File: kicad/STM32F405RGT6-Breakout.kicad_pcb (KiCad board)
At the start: 4 copper layers, 60 parts, among them J1 USB_C_Receptacle_USB2.0, J2 PWR OUT, J3 SWD/JTAG, J4 USART6, J5 SPI1, J6 I2C1, J7 I2C2, Q1 Si2301CDS, SW1 TS-1187A-B-A-B, SW2 TS-1187A-B-A-B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

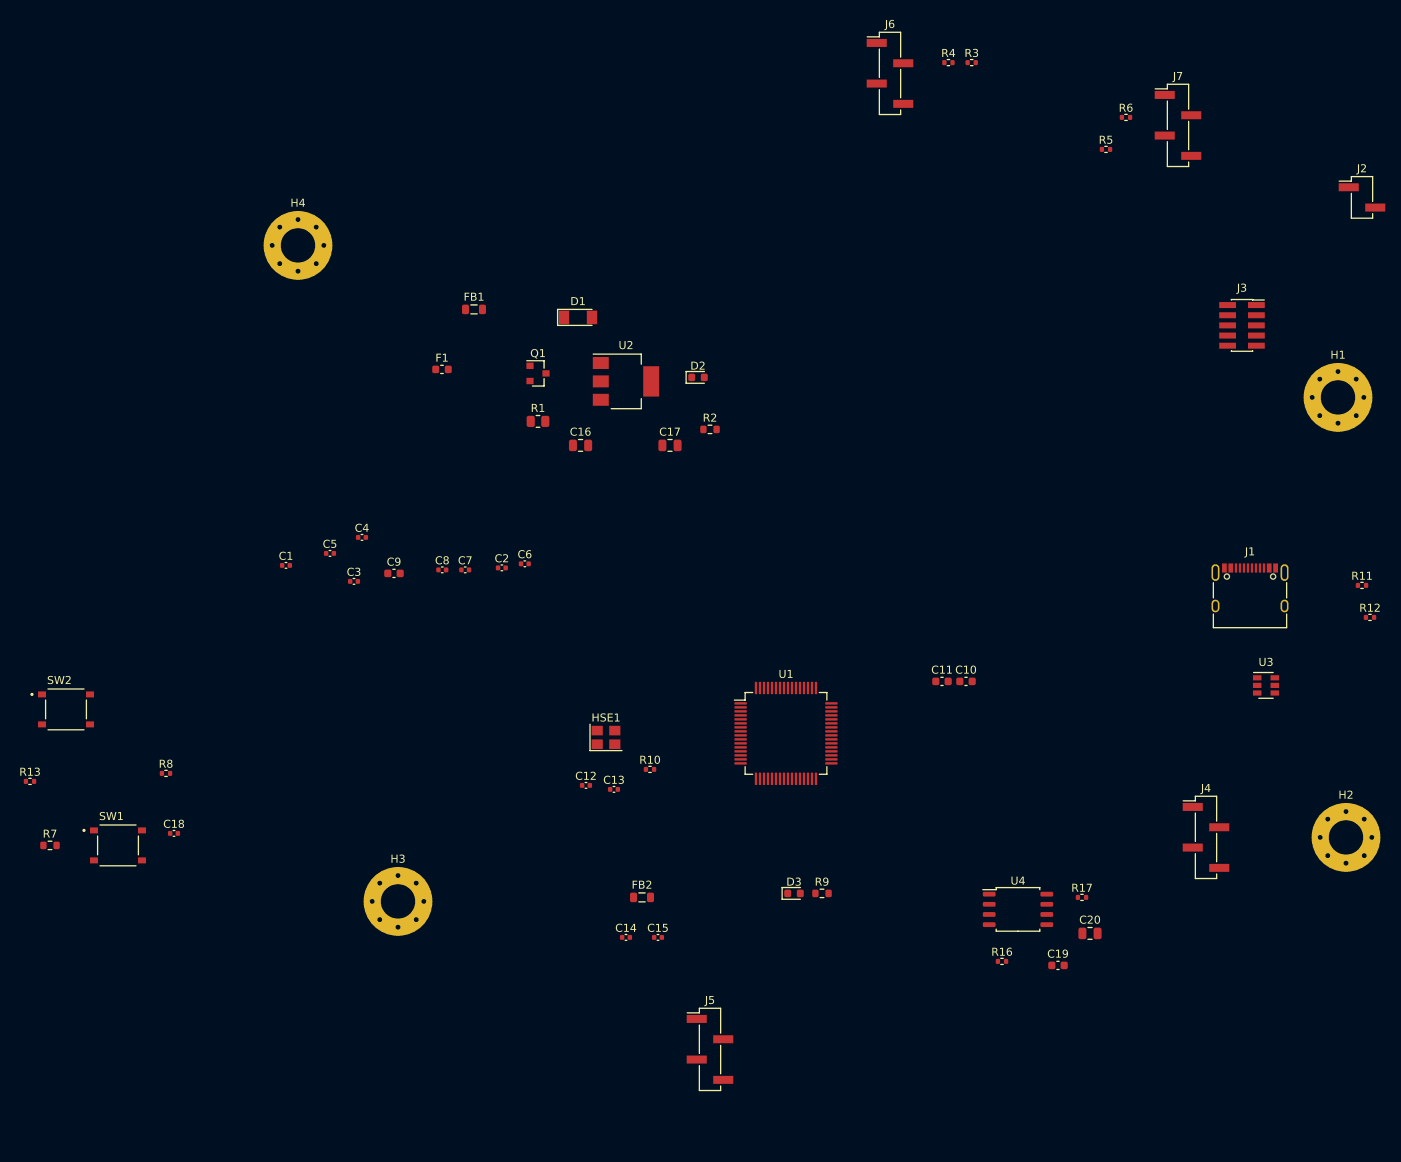
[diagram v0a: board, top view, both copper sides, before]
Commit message: - Laid out & routed crystal - Laid out & started routing MCU decoupling
--> Checkpoint before trying new flash orientation
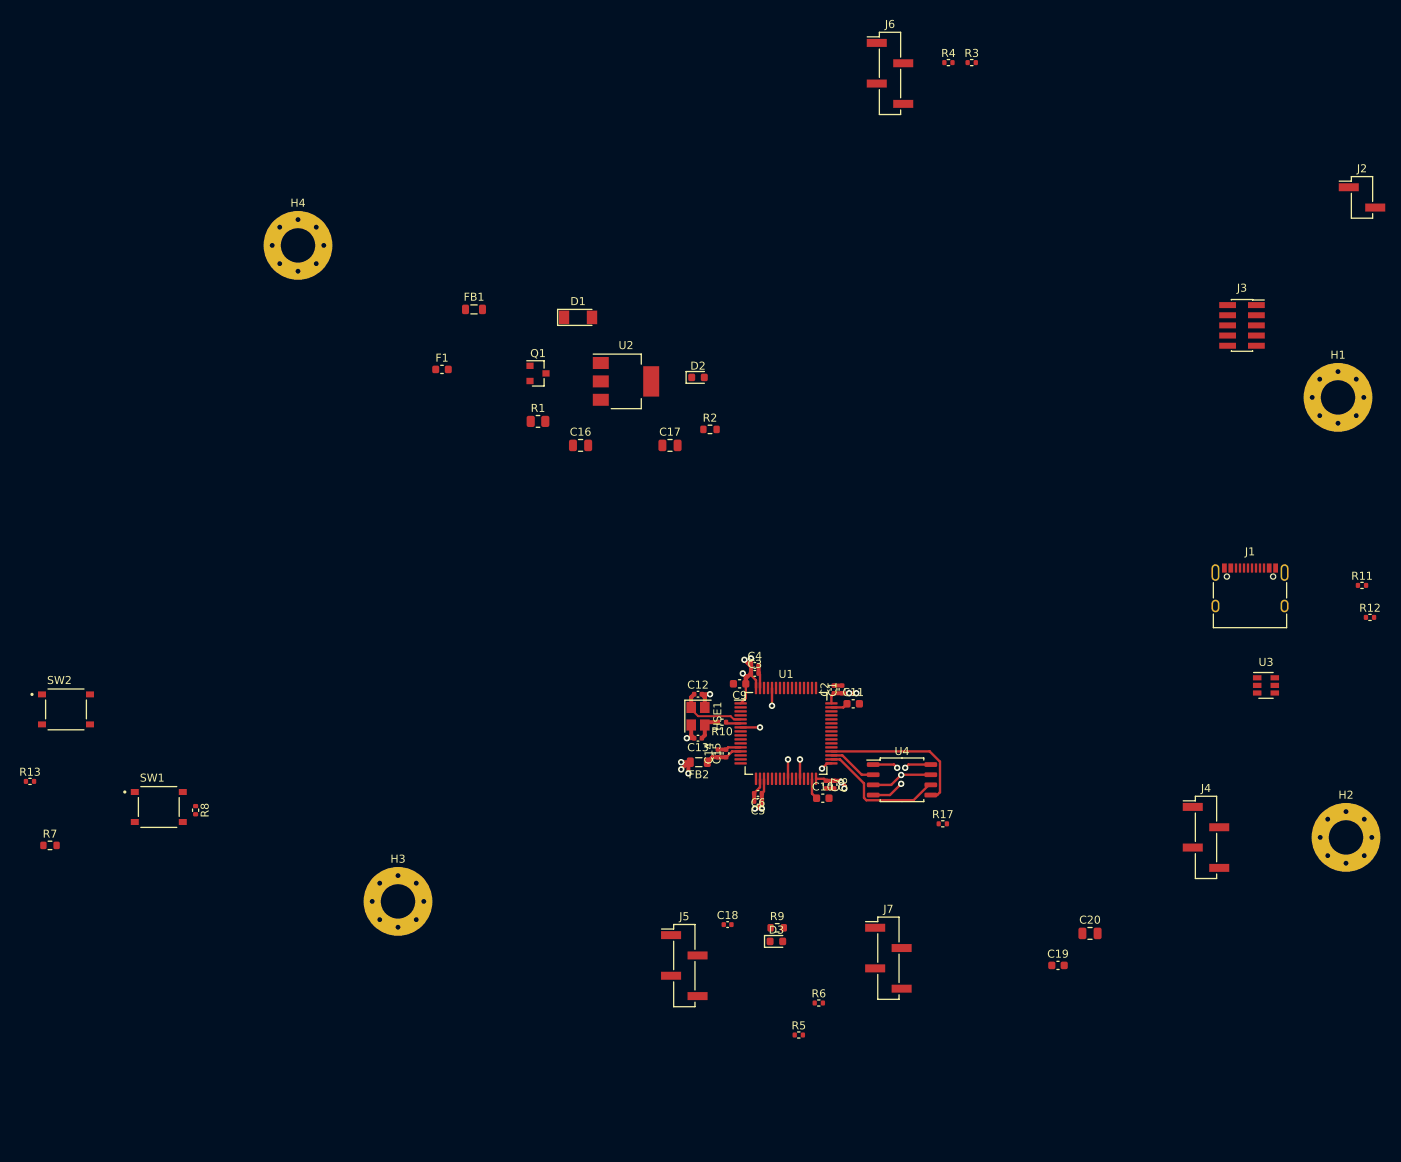
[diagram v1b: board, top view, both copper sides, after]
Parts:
- removed R16: 10k, Resistor_SMD:R_0402_1005Metric
- moved R5 117.2 mm to (123.6, 122.7)
- moved R6 117.2 mm to (126.1, 118.7)
- moved J7 110.2 mm to (134.8, 113.1)
- moved C1 71.2 mm to (129.0, 79.5), turned to 90 degrees
- moved C18 70.1 mm to (114.7, 108.9)
- moved C5 61.8 mm to (118.5, 93.5), turned to 180 degrees
- moved C8 55.8 mm to (128.0, 91.4), turned to 270 degrees
- moved C7 52.5 mm to (127.0, 91.4), turned to 270 degrees
- moved C4 51.6 mm to (118.1, 76.5)
- moved C3 51.4 mm to (118.1, 77.5)
- moved C9 45.4 mm to (116.2, 78.8), turned to 180 degrees
- moved C2 44.2 mm to (128.0, 79.5), turned to 90 degrees
- moved C6 40.9 mm to (118.5, 92.5), turned to 180 degrees
- moved C14 25.7 mm to (113.5, 87.5), turned to 90 degrees
- moved C15 24.5 mm to (114.5, 87.5), turned to 90 degrees
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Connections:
- R17 pad 1: Net-(R17-Pad1) -> GND
- R17 pad 2: GND -> Net-(R17-Pad2)
- U4 pad 3: Net-(R16-Pad2) -> Net-(R17-Pad2)
- U4 pad 7: Net-(R17-Pad1) -> Net-(R17-Pad2)
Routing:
- net +3V3: track 0.00 -> 32.1 mm, vias 0 -> 13
- net GND: track 0.00 -> 20.7 mm, vias 0 -> 3
- net FLASH_MOSI: track 0.00 -> 19.2 mm
- net FLASH_SCK: track 0.00 -> 16.4 mm
- net HSE_IN: track 0.00 -> 8.73 mm
- net Net-(R17-Pad2): track 0.00 -> 7.73 mm, vias 0 -> 1
- net FLASH_MISO: track 0.00 -> 6.23 mm
- net +3.3VA: track 0.00 -> 4.72 mm
- net FLASH_CS: track 0.00 -> 4.61 mm, vias 0 -> 2
- net Net-(C13-Pad1): track 0.00 -> 3.59 mm
- net Net-(C10-Pad1): track 0.00 -> 2.66 mm
- net Net-(D3-Pad2): track 0.00 -> 2.42 mm, vias 0 -> 1
- net NRST: track 0.00 -> 2.42 mm, vias 0 -> 1
- net BOOT1: track 0.00 -> 2.42 mm, vias 0 -> 1
- net BOOT0: track 0.00 -> 2.22 mm, vias 0 -> 1
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- added copper zone on In1.Cu, net GND
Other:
- net class 3V3 added: clearance 0.2, trace_width 0.5, via_dia 0.8, via_drill 0.4
- net class 5V added: clearance 0.2, trace_width 1, via_dia 0.8, via_drill 0.4

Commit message: This flash SPI routing is definitely better
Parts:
- moved R17 7.83 mm to (142.3, 88.5), turned to 180 degrees
- moved U4 1.70 mm to (136.5, 89.1), turned to 180 degrees
- moved C10 0.10 mm to (126.5, 93.1)
- moved C7 0.10 mm to (126.9, 91.4)
- moved C8 0.10 mm to (127.9, 91.4)
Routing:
- net FLASH_MOSI: track 19.2 -> 5.25 mm
- net FLASH_MISO: track 6.23 -> 17.7 mm
- net FLASH_SCK: track 16.4 -> 5.31 mm
- net GND: track 20.7 -> 16.6 mm, vias 3 -> 2
- net Net-(R17-Pad2): track 7.73 -> 9.67 mm, vias 1 -> 0
- net +3V3: track 32.1 -> 30.2 mm
- net FLASH_CS: track 4.61 -> 6.40 mm

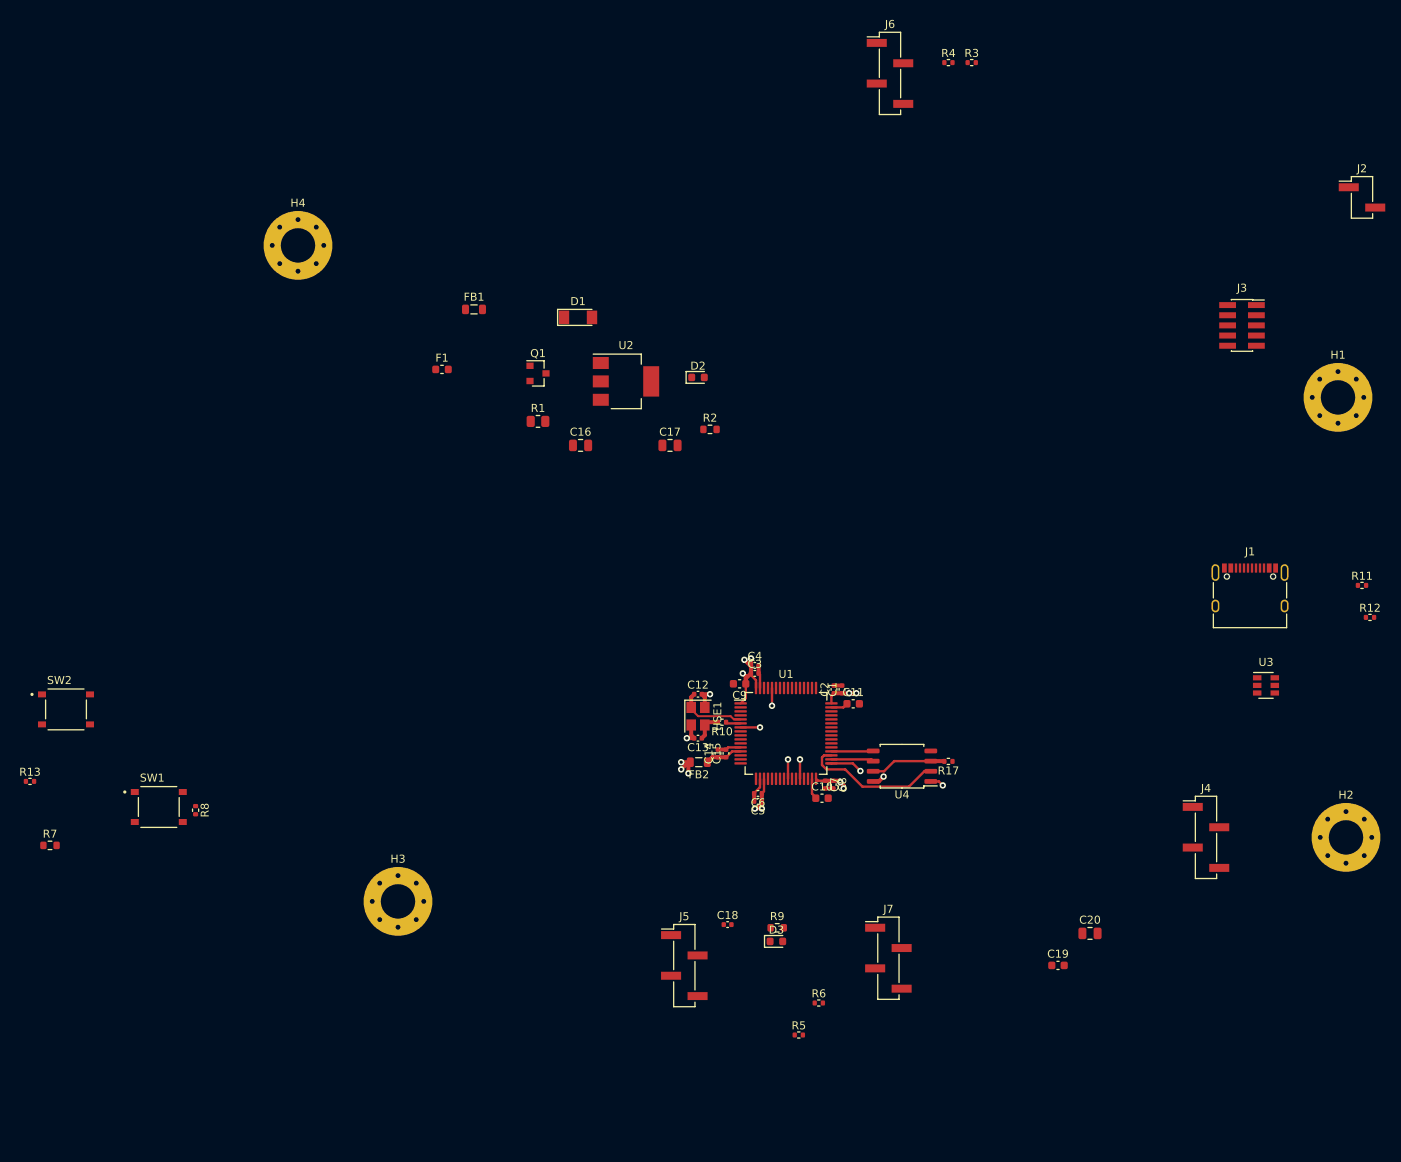
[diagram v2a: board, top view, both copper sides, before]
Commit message: - USB connector & ESD protection laid out - Crystal moved to make room for fanning out GPIO pins
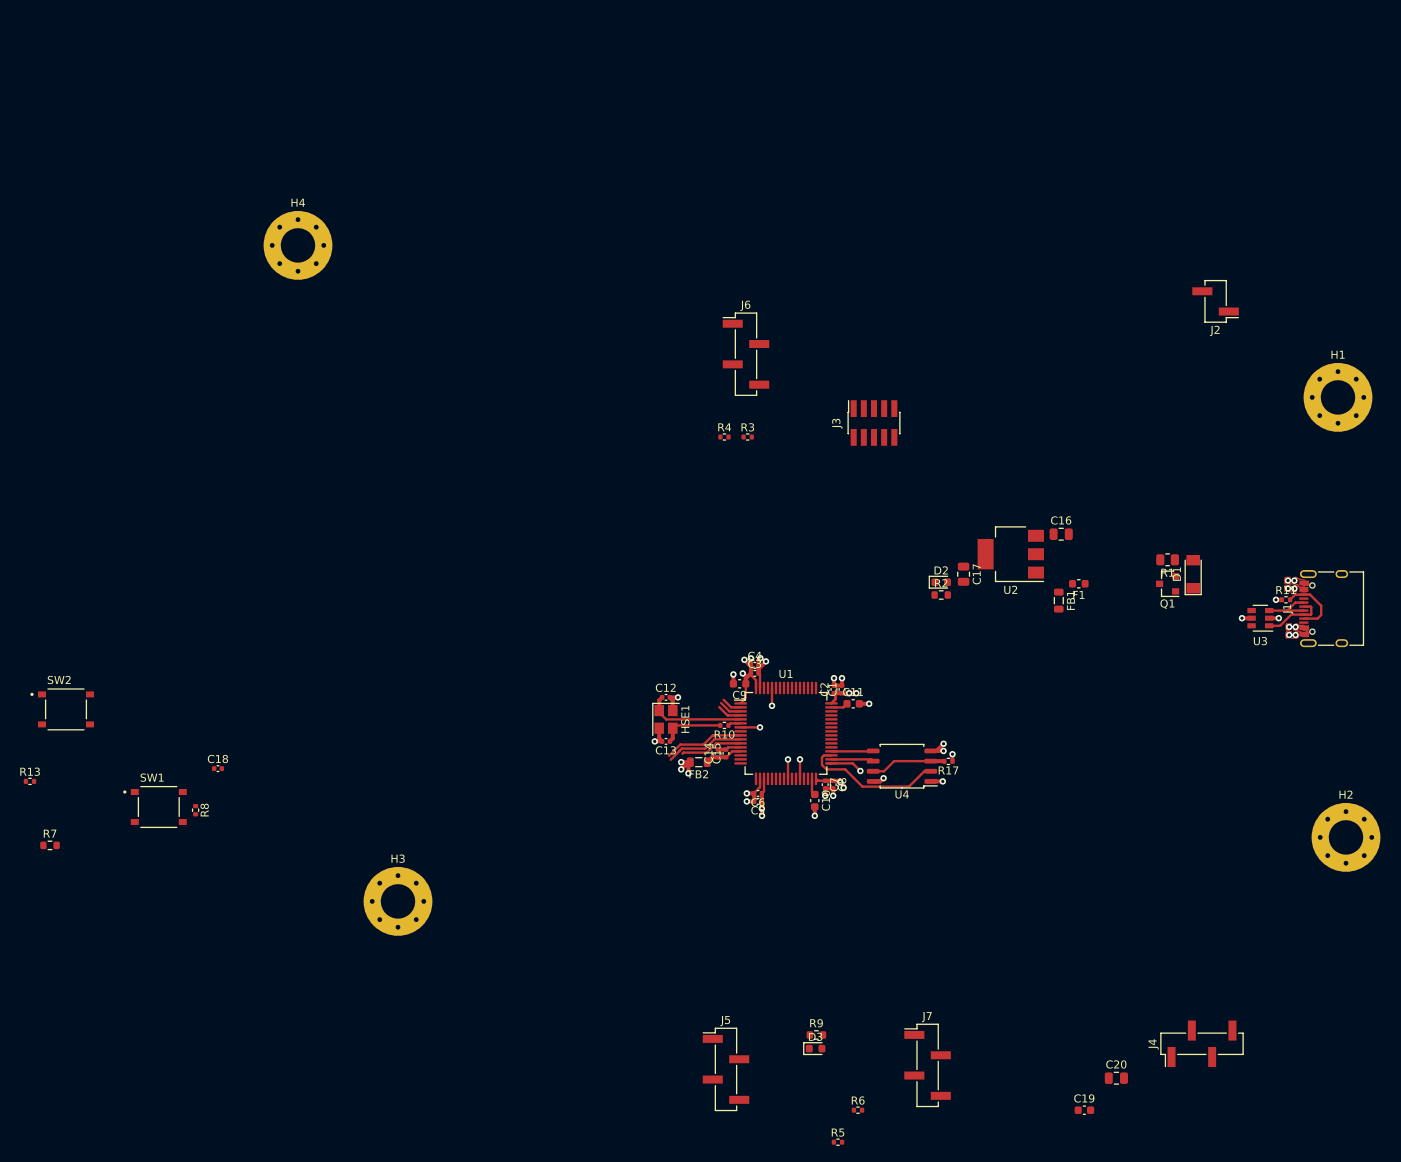
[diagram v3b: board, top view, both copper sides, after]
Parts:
- removed R12: 5.1k, Resistor_SMD:R_0402_1005Metric
- moved F1 84.0 mm to (158.6, 66.3), turned to 180 degrees
- moved D1 83.3 mm to (172.9, 65.1), turned to 90 degrees
- moved Q1 83.0 mm to (169.7, 66.3), turned to 180 degrees
- moved FB1 81.7 mm to (156.1, 68.4), turned to 270 degrees
- moved R1 80.6 mm to (169.7, 63.3), turned to 180 degrees
- moved C18 66.6 mm to (51.0, 89.4)
- moved C16 61.1 mm to (156.4, 60.1)
- moved R3 54.5 mm to (117.2, 48.0)
- moved R4 54.5 mm to (114.3, 48.0)
- moved U2 52.7 mm to (150.1, 62.6), turned to 180 degrees
- moved J3 47.6 mm to (133.0, 46.2), turned to 90 degrees
- moved C17 40.1 mm to (144.2, 65.1), turned to 270 degrees
- moved D2 39.7 mm to (141.4, 66.1)
- moved J6 39.4 mm to (117.0, 37.6)
- moved R2 35.5 mm to (141.4, 67.7)
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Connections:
- J1 pad B5: Net-(J1-PadB5) -> Net-(J1-PadA5)
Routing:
- net GND: track 16.6 -> 35.0 mm, vias 2 -> 22
- net Net-(U1-Pad9): track 0.00 -> 10.00 mm
- net Net-(U1-Pad10): track 0.00 -> 9.79 mm
- net Net-(J1-PadA5): track 0.00 -> 8.25 mm
- net Net-(U1-Pad11): track 0.00 -> 7.81 mm
- net USB_CONN_D-: track 0.00 -> 7.69 mm
- net USB_CONN_D+: track 0.00 -> 6.81 mm
- net Net-(C13-Pad1): track 3.59 -> 8.52 mm
- net HSE_IN: track 8.73 -> 12.6 mm
- net Net-(U1-Pad4): track 0.00 -> 3.11 mm
- net Net-(U1-Pad3): track 0.00 -> 2.86 mm
- net Net-(U1-Pad2): track 0.00 -> 2.52 mm
- net +5V: track 0.00 -> 1.20 mm, vias 0 -> 5
- net +3V3: track 30.2 -> 31.4 mm
- net Net-(C10-Pad1): track 2.66 -> 2.09 mm
- added copper zone on F.Cu, net +5V
- added copper zone on F.Cu, net GND
- removed copper zone on In1.Cu, net GND
